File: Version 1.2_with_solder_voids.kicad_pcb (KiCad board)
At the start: 4 copper layers, 35.1 x 39.2 mm, 33 parts, among them J1 Conn_01x04_Pin, J2 Conn_01x02_Pin, J3 Conn_01x07_Pin, J4 Conn_Coaxial, U1 BGA2801, U2 BGA420, U3 AS179-92LF, U4 SX1278, U5 74LVC1G19, Y1 ECS-TXO-2520-33-400-AN-TR

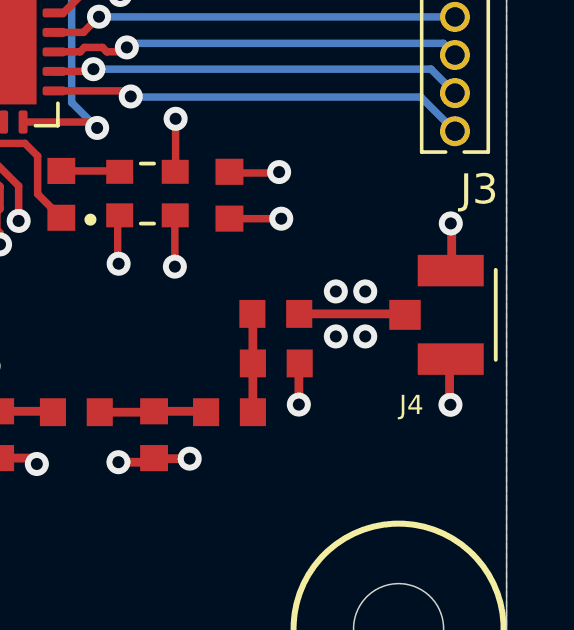
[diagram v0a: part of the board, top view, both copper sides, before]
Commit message: Added a version with and without solder voids.
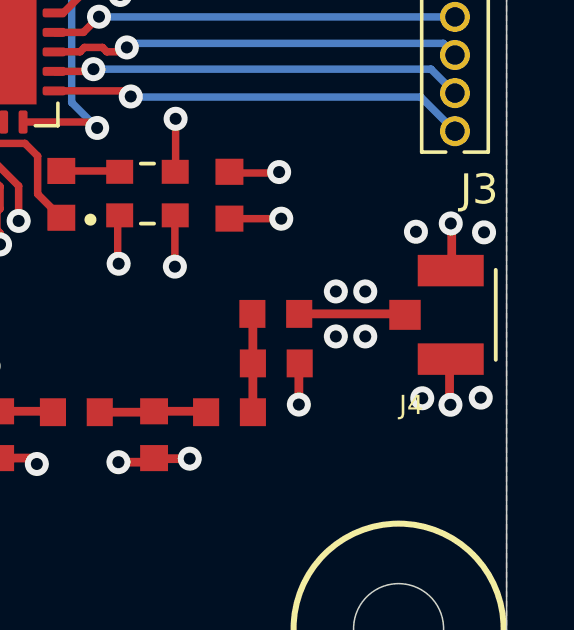
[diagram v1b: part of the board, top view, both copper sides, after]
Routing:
- net GND: vias 37 -> 41
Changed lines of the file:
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@@
   (via (at 138.2034 98.0212) (size 0.8) (drill 0.4) (layers "F.Cu" "B.Cu") (net 2))
   (via (at 133.8178 81.2474) (size 0.8) (drill 0.4) (layers "F.Cu" "B.Cu") (net 2))
+  (via (at 155.63 89.96) (size 0.8) (drill 0.4) (layers "F.Cu" "B.Cu") (free) (net 2))
   (via (at 141.0314 78.5804) (size 0.8) (drill 0.4) (layers "F.Cu" "B.Cu") (net 2))
   (via (at 126.2473 80.7872) (size 0.8) (drill 0.4) (layers "F.Cu" "B.Cu") (net 2))
@@
   (via (at 150.69 91.93) (size 0.8) (drill 0.4) (layers "F.Cu" "B.Cu") (free) (net 2))
   (via (at 124.2877 89.4318) (size 0.8) (drill 0.4) (layers "F.Cu" "B.Cu") (net 2))
+  (via (at 153.57 95.49) (size 0.8) (drill 0.4) (layers "F.Cu" "B.Cu") (free) (net 2))
   (via (at 134.2106 84.498815) (size 0.8) (drill 0.4) (layers "F.Cu" "B.Cu") (net 2))
   (via (at 134.595 95.965) (size 0.8) (drill 0.4) (layers "F.Cu" "B.Cu") (net 2))
   (via (at 134.21 87.04) (size 0.8) (drill 0.4) (layers "F.Cu" "B.Cu") (free) (net 2))
+  (via (at 153.36 89.94) (size 0.8) (drill 0.4) (layers "F.Cu" "B.Cu") (free) (net 2))
   (via (at 133.72 89.97) (size 0.8) (drill 0.4) (layers "F.Cu" "B.Cu") (free) (net 2))
   (via (at 154.5101 95.7072) (size 0.8) (drill 0.4) (layers "F.Cu" "B.Cu") (net 2))
@@
   (via (at 143.4434 97.6212) (size 0.8) (drill 0.4) (layers "F.Cu" "B.Cu") (net 2))
   (via (at 140.7234 97.6812) (size 0.8) (drill 0.4) (layers "F.Cu" "B.Cu") (free) (net 2))
+  (via (at 155.52 95.47) (size 0.8) (drill 0.4) (layers "F.Cu" "B.Cu") (free) (net 2))
   (segment (start 154.4741 90.8997) (end 154.4629 90.8885) (width 0.25) (layer "In1.Cu") (net 2))
   (segment (start 134.7978 69.3368) (end 134.7978 71.0028) (width 0.29337) (layer "In1.Cu") (net 2))
@@
       )
     )
+  )
+  (zone (net 0) (net_name "") (layers "F.Cu" "F.SilkS") (hatch edge 0.5)
+    (connect_pads (clearance 0))
+    (min_thickness 0.25) (filled_areas_thickness no)
+    (keepout (tracks not_allowed) (vias not_allowed) (pads not_allowed) (copperpour not_allowed) (footprints allowed))
+    (fill (thermal_gap 0.5) (thermal_bridge_width 0.5))
+    (polygon
+      (pts
+        (xy 131.359736 90.628878)
+        (xy 131.359736 89.568878)
+        (xy 132.159736 89.558878)
+        (xy 132.159736 90.628878)
+      )
+    )
+  )
+  (zone (net 0) (net_name "") (layers "F.Cu" "F.SilkS") (hatch edge 0.5)
+    (connect_pads (clearance 0))
+    (min_thickness 0.25) (filled_areas_thickness no)
+    (keepout (tracks not_allowed) (vias not_allowed) (pads not_allowed) (copperpour not_allowed) (footprints allowed))
+    (fill (thermal_gap 0.5) (thermal_bridge_width 0.5))
+    (polygon
+      (pts
+        (xy 137.938878 92.550264)
+        (xy 136.728878 92.560264)
+        (xy 136.708878 91.550264)
+        (xy 137.928878 91.540264)
+      )
+    )
+  )
+  (zone (net 0) (net_name "") (layers "F.Cu" "F.SilkS") (hatch edge 0.5)
+    (connect_pads (clearance 0))
+    (min_thickness 0.25) (filled_areas_thickness no)
+    (keepout (tracks not_allowed) (vias not_allowed) (pads not_allowed) (copperpour not_allowed) (footprints allowed))
+    (fill (thermal_gap 0.5) (thermal_bridge_width 0.5))
+    (polygon
+      (pts
+        (xy 153.265016 93.49)
+        (xy 155.8 93.46)
+        (xy 155.79 94.908688)
+        (xy 153.24 94.948688)
+      )
+    )
+  )
+  (zone (net 0) (net_name "") (layers "F.Cu" "F.SilkS") (hatch edge 0.5)
+    (connect_pads (clearance 0))
+    (min_thickness 0.25) (filled_areas_thickness no)
+    (keepout (tracks not_allowed) (vias not_allowed) (pads not_allowed) (copperpour not_allowed) (footprints allowed))
+    (fill (thermal_gap 0.5) (thermal_bridge_width 0.5))
+    (polygon
+      (pts
+        (xy 131.38 92.55)
+        (xy 131.38 91.49)
+        (xy 132.18 91.48)
+        (xy 132.18 92.55)
+      )
+    )
+  )
+  (zone (net 0) (net_name "") (layers "F.Cu" "F.SilkS") (hatch edge 0.5)
+    (connect_pads (clearance 0))
+    (min_thickness 0.25) (filled_areas_thickness no)
+    (keepout (tracks not_allowed) (vias not_allowed) (pads not_allowed) (copperpour not_allowed) (footprints allowed))
+    (fill (thermal_gap 0.5) (thermal_bridge_width 0.5))
+    (polygon
+      (pts
+        (xy 135.41 95.54)
+        (xy 136.47 95.54)
+        (xy 136.48 96.34)
+        (xy 135.41 96.34)
+      )
+    )
+  )
+  (zone (net 0) (net_name "") (layers "F.Cu" "F.SilkS") (hatch edge 0.5)
+    (connect_pads (clearance 0))
+    (min_thickness 0.25) (filled_areas_thickness no)
+    (keepout (tracks not_allowed) (vias not_allowed) (pads not_allowed) (copperpour not_allowed) (footprints allowed))
+    (fill (thermal_gap 0.5) (thermal_bridge_width 0.5))
+    (polygon
+      (pts
+        (xy 138.825016 96.811312)
+        (xy 140.18 96.811312)
+        (xy 140.18 98.14)
+        (xy 138.81 98.15)
+      )
+    )
+  )
+  (zone (net 0) (net_name "") (layers "F.Cu" "F.SilkS") (hatch edge 0.5)
+    (connect_pads (clearance 0))
+    (min_thickness 0.25) (filled_areas_thickness no)
+    (keepout (tracks not_allowed) (vias not_allowed) (pads not_allowed) (copperpour not_allowed) (footprints allowed))
+    (fill (thermal_gap 0.5) (thermal_bridge_width 0.5))
+    (polygon
+      (pts
+        (xy 132.119736 90.618878)
+        (xy 132.119736 89.558878)
+        (xy 132.919736 89.548878)
+        (xy 132.919736 90.618878)
+      )
+    )
+  )
+  (zone (net 0) (net_name "") (layers "F.Cu" "F.SilkS") (hatch edge 0.5)
+    (connect_pads (clearance 0))
+    (min_thickness 0.25) (filled_areas_thickness no)
+    (keepout (tracks not_allowed) (vias not_allowed) (pads not_allowed) (copperpour not_allowed) (footprints allowed))
+    (fill (thermal_gap 0.5) (thermal_bridge_width 0.5))
+    (polygon
+      (pts
+        (xy 153.265016 90.51)
+        (xy 155.8 90.48)
+        (xy 155.79 91.928688)
+        (xy 153.24 91.968688)
+      )
+    )
+  )
+  (zone (net 0) (net_name "") (layers "F.Cu" "F.SilkS") (hatch edge 0.5)
+    (connect_pads (clearance 0))
+    (min_thickness 0.25) (filled_areas_thickness no)
+    (keepout (tracks not_allowed) (vias not_allowed) (pads not_allowed) (copperpour not_allowed) (footprints allowed))
+    (fill (thermal_gap 0.5) (thermal_bridge_width 0.5))
+    (polygon
+      (pts
+        (xy 143.955016 96.81)
+        (xy 145.31 96.81)
+        (xy 145.31 98.138688)
+        (xy 143.94 98.148688)
+      )
+    )
+  )
+  (zone (net 0) (net_name "") (layers "F.Cu" "F.SilkS") (hatch edge 0.5)
+    (connect_pads (clearance 0))
+    (min_thickness 0.25) (filled_areas_thickness no)
+    (keepout (tracks not_allowed) (vias not_allowed) (pads not_allowed) (copperpour not_allowed) (footprints allowed))
+    (fill (thermal_gap 0.5) (thermal_bridge_width 0.5))
+    (polygon
+      (pts
+        (xy 148.815016 93.67)
+        (xy 150.17 93.67)
+        (xy 150.17 94.998688)
+        (xy 148.8 95.008688)
+      )
+    )
